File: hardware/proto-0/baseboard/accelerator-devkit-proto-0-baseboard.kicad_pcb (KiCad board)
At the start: 6 copper layers, 50 x 42 mm, 175 parts, among them J1 JTAG, J2 USB-C, J3 HDMI, J4 Qwiic I2C, J5 Pmod 1A, J6 Pmod 1B, J7 Display, J8 microSD-ST11-H, Q1 CSD13381F4, SW1 BUTTON1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

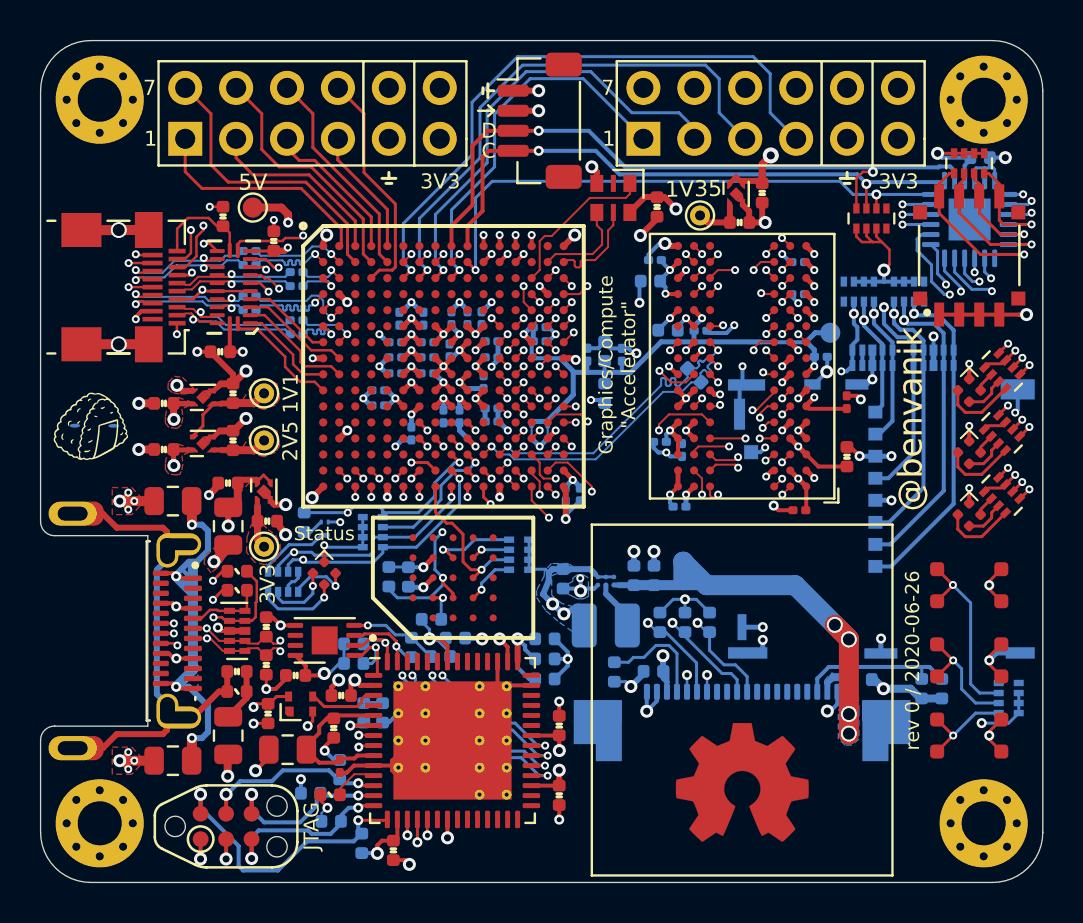
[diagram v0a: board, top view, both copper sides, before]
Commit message: Moving all power rail test points to the front
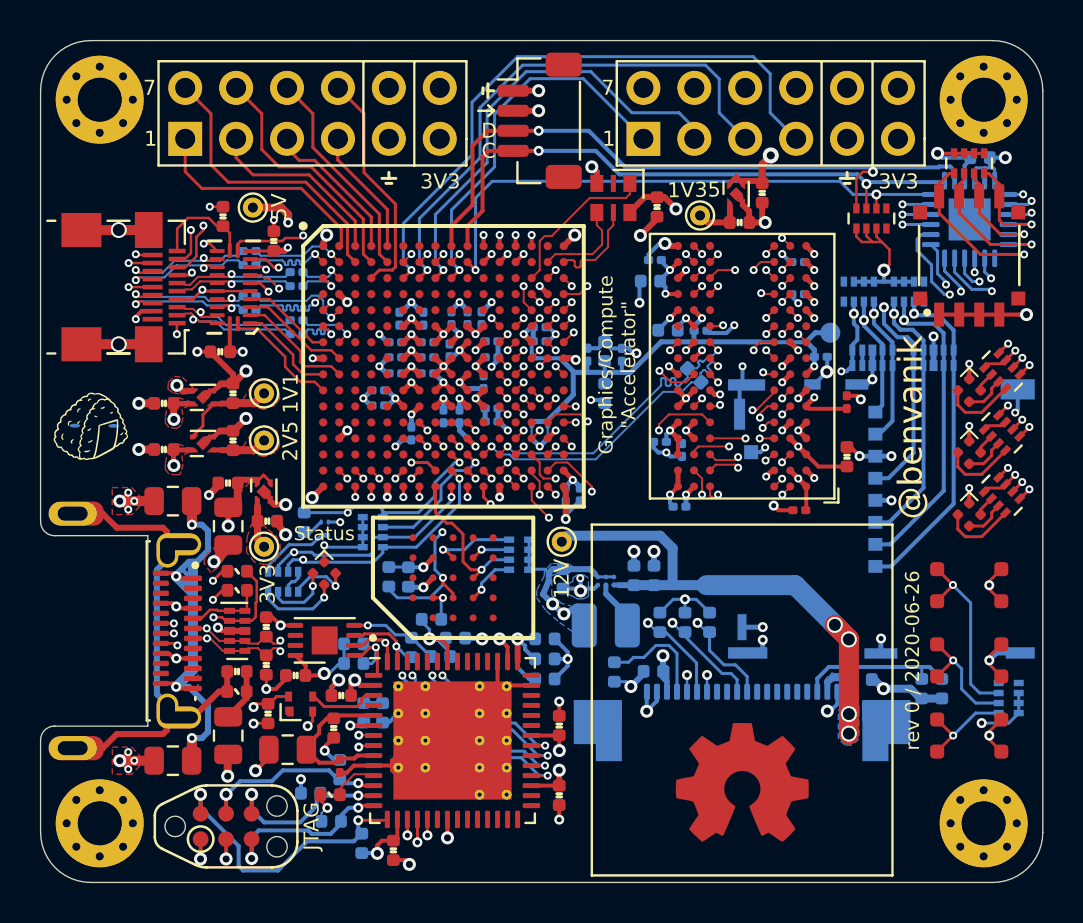
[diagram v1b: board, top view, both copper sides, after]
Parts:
- TP2: footprint TestPoint:TestPoint_Pad_D1.0mm -> TestPoint:TestPoint_THTPad_D1.0mm_Drill0.5mm; moved to F.Cu
- TP6: footprint TestPoint:TestPoint_Pad_D1.0mm -> TestPoint:TestPoint_THTPad_D1.0mm_Drill0.5mm
- moved TP2 6.15 mm to (30.0, 32.0), turned to -90 degrees
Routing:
- net +12V: track 29.9 -> 33.6 mm
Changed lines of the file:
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@@
     (thickness 1.6)
     (drawings 36)
-    (tracks 4030)
+    (tracks 4027)
     (modules 175)
     (nets 346)
@@
       (dielectric_constraints yes)
     )
-    (last_trace_width 0.2)
+    (last_trace_width 0.3)
     (user_trace_width 0.09)
     (user_trace_width 0.1)
@@
     (add_net "/USB-I/O/USB_D-")
   )
+  (module "TestPoint:TestPoint_THTPad_D1.0mm_Drill0.5mm" (layer "F.Cu")
+    (at 14.59 15.33)
+    (descr "THT pad as test Point, diameter 1.0mm, hole diameter 0.5mm")
+    (tags "test point THT pad")
+    (attr virtual)
+    (fp_text reference "TP6" (at 0 -1.448) (layer "F.SilkS") hide
+      (effects (font (size 1 1) (thickness 0.15)))
+    )
+    (fp_text value "TestPoint_Small" (at 0 1.55) (layer "F.Fab") hide
+      (effects (font (size 1 1) (thickness 0.15)))
+    )
+    (fp_circle (center 0 0) (end 0 0.7) (layer "F.SilkS") (width 0.12))
+    (fp_circle (center 0 0) (end 1 0) (layer "F.CrtYd") (width 0.05))
+    (fp_text user "${REFERENCE}" (at 0 -1.45) (layer "F.Fab") hide
+      (effects (font (size 1 1) (thickness 0.15)))
+    )
+    (pad "1" thru_hole circle (at 0 0) (size 1 1) (drill 0.5) (layers *.Cu *.Mask)
+      (net 1 "+5V") (pinfunction "1"))
+  )
+  (module "TestPoint:TestPoint_THTPad_D1.0mm_Drill0.5mm" (layer "F.Cu")
+    (at 30 32 -90)
+    (descr "THT pad as test Point, diameter 1.0mm, hole diameter 0.5mm")
+    (tags "test point THT pad")
+    (attr virtual)
+    (fp_text reference "TP2" (at 0 -1.448 -90) (layer "F.SilkS") hide
+      (effects (font (size 1 1) (thickness 0.15)))
+    )
+    (fp_text value "TestPoint_Small" (at 0 1.55 -90) (layer "F.Fab") hide
+      (effects (font (size 1 1) (thickness 0.15)))
+    )
+    (fp_circle (center 0 0) (end 0 0.7) (layer "F.SilkS") (width 0.12))
+    (fp_circle (center 0 0) (end 1 0) (layer "F.CrtYd") (width 0.05))
+    (fp_text user "${REFERENCE}" (at 0 -1.45 -90) (layer "F.Fab") hide
+      (effects (font (size 1 1) (thickness 0.15)))
+    )
+    (pad "1" thru_hole circle (at 0 0 270) (size 1 1) (drill 0.5) (layers *.Cu *.Mask)
+      (net 271 "+12V") (pinfunction "1"))
+  )
   (module "Connector_JST_RD:Qwiic_JST_SH_BM04B-SRSS-TB_1x04-1MP_P1.00mm_Vertical" locked (layer "F.Cu")
     (at 28.9 11 -90)
@@
       (xy 0.555814 -2.531069)) (layer "F.Cu") (width 0.01))
   )
-  (module "TestPoint:TestPoint_Pad_D1.0mm" (layer "F.Cu")
-    (at 14.59 15.33)
-    (descr "SMD pad as test Point, diameter 1.0mm")
-    (tags "test point SMD pad")
-    (attr virtual)
-    (fp_text reference "TP6" (at 0 -1.448) (layer "F.SilkS") hide
-      (effects (font (size 1 1) (thickness 0.15)))
-    )
-    (fp_text value "TestPoint_Small" (at 0 1.55) (layer "F.Fab") hide
-      (effects (font (size 1 1) (thickness 0.15)))
-    )
-    (fp_circle (center 0 0) (end 0 0.7) (layer "F.SilkS") (width 0.12))
-    (fp_circle (center 0 0) (end 1 0) (layer "F.CrtYd") (width 0.05))
-    (fp_text user "${REFERENCE}" (at 0 -1.45) (layer "F.Fab") hide
-      (effects (font (size 1 1) (thickness 0.15)))
-    )
-    (pad "1" smd circle (at 0 0) (size 1 1) (layers "F.Cu" "F.Mask")
-      (net 1 "+5V") (pinfunction "1"))
-  )
-  (module "TestPoint:TestPoint_Pad_D1.0mm" (layer "B.Cu")
-    (at 36.07 33 180)
-    (descr "SMD pad as test Point, diameter 1.0mm")
-    (tags "test point SMD pad")
-    (attr virtual)
-    (fp_text reference "TP2" (at 0 1.448) (layer "B.SilkS") hide
-      (effects (font (size 1 1) (thickness 0.15)) (justify mirror))
-    )
-    (fp_text value "TestPoint_Small" (at 0 -1.55) (layer "B.Fab") hide
-      (effects (font (size 1 1) (thickness 0.15)) (justify mirror))
-    )
-    (fp_circle (center 0 0) (end 0 -0.7) (layer "B.SilkS") (width 0.12))
-    (fp_circle (center 0 0) (end 1 0) (layer "B.CrtYd") (width 0.05))
-    (fp_text user "${REFERENCE}" (at 0 1.45) (layer "B.Fab") hide
-      (effects (font (size 1 1) (thickness 0.15)) (justify mirror))
-    )
-    (pad "1" smd circle (at 0 0 180) (size 1 1) (layers "B.Cu" "B.Mask")
-      (net 271 "+12V") (pinfunction "1"))
-  )
   (module "Button_Switch_SMD_RD:CVS-04TB" (layer "F.Cu")
     (at 50.33 17.72 90)
@@
     (effects (font (size 0.8 0.8) (thickness 0.135)) (justify left mirror))
   )
-  (gr_text "@benvanik" (at 47.4 25.9 90) (layer "F.SilkS")
+  (gr_text "@benvanik" (at 47.4 26.3 90) (layer "F.SilkS")
     (effects (font (size 1.2 1.2) (thickness 0.2)))
   )
   (gr_text "VTT_REF" (at 46.31 21.59) (layer "B.SilkS")
-    (effects (font (size 0.75 0.75) (thickness 0.1)) (justify mirror))
+    (effects (font (size 0.75 0.75) (thickness 0.135)) (justify mirror))
   )
-  (gr_text "12V" (at 37.41 33 90) (layer "B.SilkS")
-    (effects (font (size 0.75 0.75) (thickness 0.1)) (justify mirror))
+  (gr_text "12V" (at 30 33.85 90) (layer "F.SilkS")
+    (effects (font (size 0.75 0.75) (thickness 0.135)))
   )
   (gr_text "JTAG" (at 17.52 46.2 90) (layer "F.SilkS")
     (effects (font (size 0.75 0.75) (thickness 0.1)))
   )
-  (gr_text "5V" (at 14.59 14.07) (layer "F.SilkS")
-    (effects (font (size 0.8 0.8) (thickness 0.135)))
+  (gr_text "5V" (at 15.9 15.3 90) (layer "F.SilkS")
+    (effects (font (size 0.75 0.75) (thickness 0.135)))
   )
-  (gr_text "1V35" (at 36.58 14.4 1) (layer "F.SilkS")
-    (effects (font (size 0.8 0.8) (thickness 0.135)))
+  (gr_text "1V35" (at 36.6 14.45 1) (layer "F.SilkS")
+    (effects (font (size 0.75 0.75) (thickness 0.135)))
   )
   (gr_text "3V3" (at 15.33 34.11 90) (layer "F.SilkS")
-    (effects (font (size 0.75 0.75) (thickness 0.1)))
+    (effects (font (size 0.75 0.75) (thickness 0.135)))
   )
   (gr_text "2V5" (at 16.46 26.98 90) (layer "F.SilkS")
@@
     (effects (font (size 0.7 0.7) (thickness 0.15)))
   )
-  (gr_text "@benvanik" (at 47.4 25.9 90) (layer "F.Cu")
+  (gr_text "@benvanik" (at 47.4 26.3 90) (layer "F.Cu")
     (effects (font (size 1.2 1.2) (thickness 0.2)))
   )
@@
   (gr_line (start 6.5 49) (end 51.5 49) (layer "Edge.Cuts") (width 0.05))
   (gr_line (start 4 9.5) (end 4 31) (layer "Edge.Cuts") (width 0.05))
+  (segment (start 35.53 34.17) (end 35.53 32.32) (width 0.5) (layer "B.Cu") (net 271))
+  (segment (start 34.91 31.7) (end 30.25 31.7) (width 0.5) (layer "B.Cu") (net 271))
+  (segment (start 35.53 32.32) (end 34.91 31.7) (width 0.5) (layer "B.Cu") (net 271))
+  (segment (start 34.60309 34.17) (end 37.62 34.17) (width 0.5) (layer "B.Cu") (net 271))
   (segment (start 34.54 38.17) (end 36.767002 38.17) (width 0.127) (layer "In3.Cu") (net 273))
   (segment (start 36.767002 38.17) (end 36.768501 38.168501) (width 0.127) (layer "In3.Cu") (net 273))
   (segment (start 29.19701 36.93701) (end 33.30701 36.93701) (width 0.127) (layer "In3.Cu") (net 273))
   (segment (start 33.30701 36.93701) (end 34.54 38.17) (width 0.127) (layer "In3.Cu") (net 273))
-  (segment (start 33.47 36.66) (end 33.64 36.66) (width 0.127) (layer "In3.Cu") (net 259))
+  (segment (start 29.39 36.66) (end 33.64 36.66) (width 0.127) (layer "In3.Cu") (net 259))
   (segment (start 33.64 36.66) (end 34.191499 37.211499) (width 0.127) (layer "In3.Cu") (net 259))
   (segment (start 34.191499 37.211499) (end 35.613501 37.211499) (width 0.127) (layer "In3.Cu") (net 259))
@@
   (segment (start 23.225 35.475) (end 28.735 35.475) (width 0.127) (layer "In3.Cu") (net 253))
   (segment (start 28.735 35.475) (end 29.63 36.37) (width 0.127) (layer "In3.Cu") (net 253))
-  (segment (start 29.39 36.66) (end 33.47 36.66) (width 0.127) (layer "In3.Cu") (net 259))
   (segment (start 28.505 35.775) (end 29.39 36.66) (width 0.127) (layer "In3.Cu") (net 259))
   (segment (start 23.075 35.775) (end 28.505 35.775) (width 0.127) (layer "In3.Cu") (net 259))
@@
   (segment (start 42.175 22.05) (end 42.2 22.025) (width 0.2) (layer "B.Cu") (net 6))
   (via (at 30.7 22.93) (size 0.5) (drill 0.25) (layers "F.Cu" "B.Cu") (net 211))
-  (segment (start 36.07 33.91) (end 36.07 33.04) (width 0.5) (layer "B.Cu") (net 271))
-  (segment (start 36.07 34.17) (end 36.07 33.91) (width 0.5) (layer "B.Cu") (net 271))
-  (segment (start 36.07 33) (end 36.07 33.91) (width 1) (layer "B.Cu") (net 271))
   (segment (start 37.22 34.17) (end 41.645 34.17) (width 1) (layer "B.Cu") (net 271))
-  (segment (start 37.22 34.17) (end 36.05 33) (width 1) (layer "B.Cu") (net 271))
   (segment (start 16.35 16.075) (end 16.35 15.675) (width 0.4) (layer "F.Cu") (net 1))
   (segment (start 16.35 15.675) (end 16.01 15.33) (width 0.4) (layer "F.Cu") (net 1))
@@
   (segment (start 22.1 22.85) (end 22.5 22.45) (width 0.25) (layer "F.Cu") (net 219))
   (segment (start 22.9 22.85) (end 22.5 22.45) (width 0.25) (layer "F.Cu") (net 219))
-  (segment (start 36.07 34.17) (end 37.62 34.17) (width 0.5) (layer "B.Cu") (net 271))
-  (segment (start 34.60309 34.17) (end 36.07 34.17) (width 0.5) (layer "B.Cu") (net 271))
   (segment (start 44.22 24.72) (end 44.74 24.72) (width 0.2) (layer "F.Cu") (net 211))
   (via (at 44.92 24.9) (size 0.5) (drill 0.25) (layers "F.Cu" "B.Cu") (net 211))
@@
   (segment (start 33.60309 32.48381) (end 33.60309 33.14881) (width 0.3) (layer "B.Cu") (net 211) (status 8000))
   (segment (start 33.60309 34.17) (end 34.6019 34.17) (width 0.5) (layer "B.Cu") (net 271))
-  (segment (start 32.8419 34.16) (end 33.6269 34.16) (width 0.2) (layer "B.Cu") (net 271) (status 8000))
-  (segment (start 32.60309 34.16) (end 32.8419 34.16) (width 0.25) (layer "B.Cu") (net 271) (status 8000))
+  (segment (start 32.8419 34.16) (end 33.6269 34.16) (width 0.2) (layer "B.Cu") (net 271))
+  (segment (start 32.60309 34.16) (end 32.8419 34.16) (width 0.25) (layer "B.Cu") (net 271))
   (segment (start 33.60309 34.17) (end 32.8519 34.17) (width 0.3) (layer "B.Cu") (net 271))
   (segment (start 31.6569 33.605) (end 31.8069 33.755) (width 0.2) (layer "B.Cu") (net 219) (status 8000))

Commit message: Bumping board datestamp
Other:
- board text added: "Graphics/Compute "Accelerator" Devkit"
- board text added: "rev 0 / 2020-06-27"
- board text removed: "Graphics/Compute "Accelerator""
- board text removed: "rev 0 / 2020-06-26"
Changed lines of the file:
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@@
     (effects (font (size 0.75 0.75) (thickness 0.135)))
   )
-  (gr_text "rev 0 / 2020-06-26" (at 47.5 37.925 90) (layer "F.SilkS")
+  (gr_text "rev 0 / 2020-06-27" (at 47.5 37.925 90) (layer "F.SilkS")
     (effects (font (size 0.7 0.7) (thickness 0.15)))
   )
@@
     (effects (font (size 1.2 1.2) (thickness 0.2)))
   )
-  (gr_text "Graphics/Compute\n\"Accelerator\"" (at 32.775 23.175 90) (layer "F.SilkS")
+  (gr_text "Graphics/Compute\n\"Accelerator\" Devkit" (at 32.775 23.175 90) (layer "F.SilkS")
     (effects (font (size 0.7 0.7) (thickness 0.15)))
   )

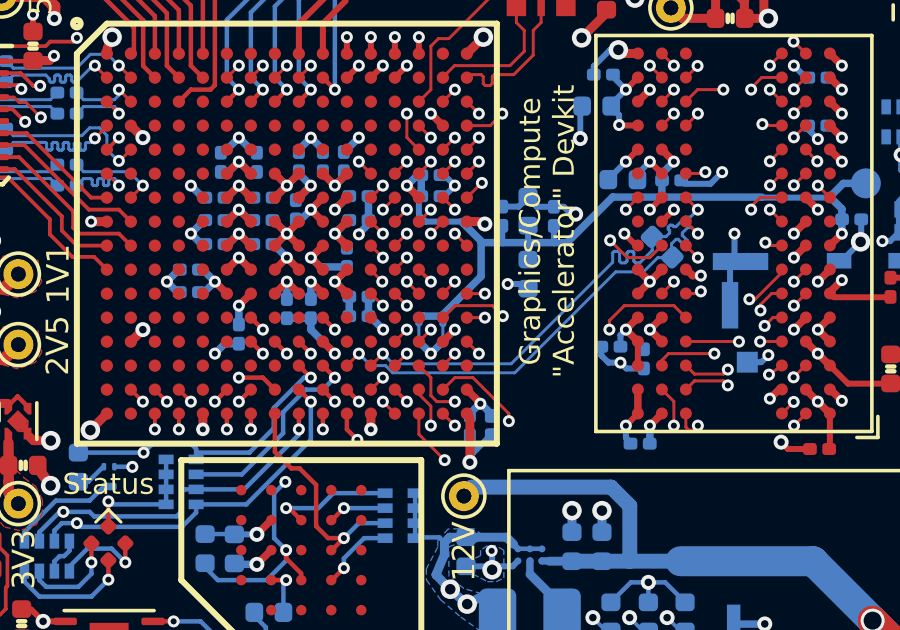
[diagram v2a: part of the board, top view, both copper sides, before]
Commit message: Removing VTT_REF roundabout
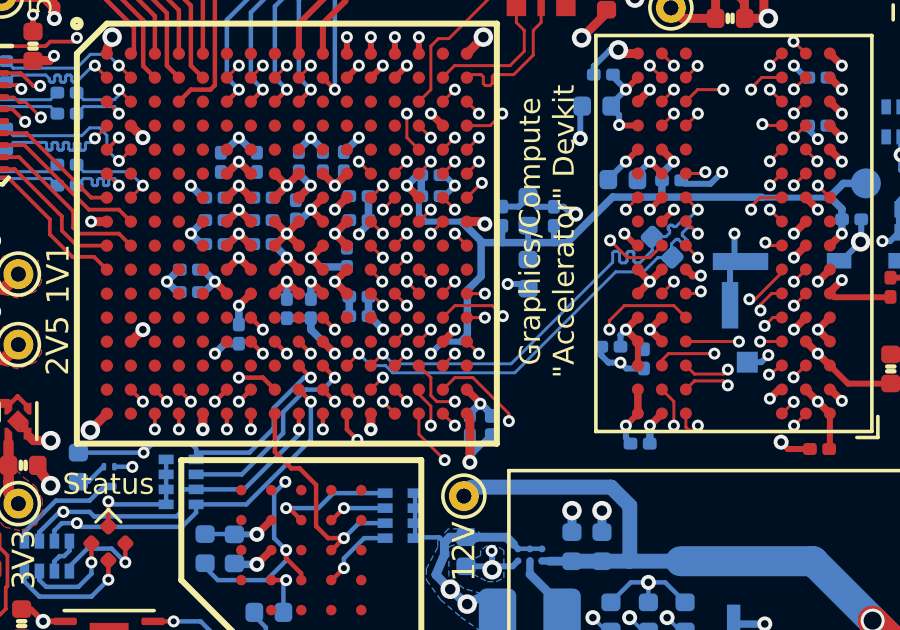
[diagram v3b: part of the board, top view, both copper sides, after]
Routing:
- net /SDRAM/VTT_REF: track 36.5 -> 34.5 mm
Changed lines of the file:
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@@
     (thickness 1.6)
     (drawings 36)
-    (tracks 4027)
+    (tracks 4021)
     (modules 175)
     (nets 346)
@@
       (dielectric_constraints yes)
     )
-    (last_trace_width 0.3)
+    (last_trace_width 0.15)
     (user_trace_width 0.09)
     (user_trace_width 0.1)
@@
   (gr_line (start 6.5 49) (end 51.5 49) (layer "Edge.Cuts") (width 0.05))
   (gr_line (start 4 9.5) (end 4 31) (layer "Edge.Cuts") (width 0.05))
+  (segment (start 30.115001 25.134999) (end 30.115001 26.634999) (width 0.25) (layer "B.Cu") (net 6))
+  (segment (start 30.575 24.675) (end 30.115001 25.134999) (width 0.25) (layer "B.Cu") (net 6))
+  (segment (start 29.3 26.85) (end 29.9 26.85) (width 0.2) (layer "B.Cu") (net 6) (status 8000))
+  (segment (start 30.115001 26.634999) (end 29.9 26.85) (width 0.25) (layer "B.Cu") (net 6) (status 8000))
   (segment (start 35.53 34.17) (end 35.53 32.32) (width 0.5) (layer "B.Cu") (net 271))
   (segment (start 34.91 31.7) (end 30.25 31.7) (width 0.5) (layer "B.Cu") (net 271))
@@
   (segment (start 31.83 22.35) (end 32.14 22.04) (width 0.2) (layer "B.Cu") (net 211))
   (segment (start 31.29 23.55) (end 32.15 23.55) (width 0.25) (layer "B.Cu") (net 6))
-  (segment (start 30.575 23.55) (end 31.29 23.55) (width 0.25) (layer "B.Cu") (net 6))
+  (segment (start 30.575 23.55) (end 31.29 23.55) (width 0.25) (layer "B.Cu") (net 6) (status 8000))
   (segment (start 31.28 22.99) (end 31.28 23.54) (width 0.2) (layer "B.Cu") (net 6))
   (segment (start 31.28 23.54) (end 31.29 23.55) (width 0.2) (layer "B.Cu") (net 6))
@@
   (segment (start 28.9 27.25) (end 30.55 28.9) (width 0.25) (layer "In3.Cu") (net 6))
   (segment (start 30.55 28.9) (end 30.55 28.92) (width 0.2) (layer "In3.Cu") (net 6))
-  (segment (start 29.3 26.772784) (end 29.3 26.85) (width 0.25) (layer "B.Cu") (net 6))
-  (segment (start 28.5 26.772784) (end 28.5 26.85) (width 0.25) (layer "B.Cu") (net 6))
-  (segment (start 28.5 26.85) (end 28.9 27.25) (width 0.25) (layer "B.Cu") (net 6))
-  (segment (start 29.3 26.85) (end 28.9 27.25) (width 0.25) (layer "B.Cu") (net 6))
-  (segment (start 29.3 26.85) (end 29.3 26.25) (width 0.1016) (layer "B.Cu") (net 6))
-  (segment (start 29.3 25.95) (end 29.3 26.25) (width 0.25) (layer "B.Cu") (net 6))
-  (segment (start 29.25 26) (end 30.575 24.675) (width 0.25) (layer "B.Cu") (net 6))
-  (segment (start 28.65 26) (end 28.5 26.15) (width 0.25) (layer "B.Cu") (net 6))
-  (segment (start 28.5 26.15) (end 28.5 26.227216) (width 0.25) (layer "B.Cu") (net 6))
-  (segment (start 28.65 26) (end 29.25 26) (width 0.25) (layer "B.Cu") (net 6))
+  (segment (start 29.3 26.85) (end 28.9 27.25) (width 0.2) (layer "B.Cu") (net 6) (status 8000))
   (segment (start 28.825 27.175) (end 28.9 27.25) (width 0.1016) (layer "B.Cu") (net 6))
   (via (at 28.9 27.25) (size 0.4) (drill 0.2) (layers "F.Cu" "B.Cu") (net 6))
-  (segment (start 28.5 26.227216) (end 28.5 26.85) (width 0.1016) (layer "B.Cu") (net 6))
   (segment (start 30.4 17.75) (end 29.7 18.45) (width 0.127) (layer "In3.Cu") (net 127))
   (segment (start 30.376818 20.45) (end 29.976818 20.85) (width 0.127) (layer "In3.Cu") (net 136))
